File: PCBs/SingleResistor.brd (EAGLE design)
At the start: 10.2 x 39.5 mm, 3 parts

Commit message: Updated
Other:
- board size 10.2 x 39.5 mm -> 15 x 39.2 mm
- board text added: "PinwheelRobotics"
- board text added: "care@pinwheel.in"
- board text removed: "Pinwheel Robotics"
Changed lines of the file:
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@@
 <setting verticaltext="up"/>
 </settings>
-<grid distance="50" unitdist="mil" unit="mm" style="lines" multiple="1" display="yes" altdistance="5" altunitdist="mil" altunit="mm"/>
+<grid distance="0.5" unitdist="mm" unit="mm" style="lines" multiple="1" display="yes" altdistance="5" altunitdist="mil" altunit="mm"/>
 <layers>
 <layer number="1" name="Top" color="4" fill="1" visible="yes" active="yes"/>
@@
 <layer number="43" name="vRestrict" color="2" fill="10" visible="yes" active="yes"/>
 <layer number="44" name="Drills" color="7" fill="1" visible="no" active="yes"/>
-<layer number="45" name="Holes" color="7" fill="1" visible="no" active="yes"/>
+<layer number="45" name="Holes" color="7" fill="1" visible="yes" active="yes"/>
 <layer number="46" name="Milling" color="3" fill="1" visible="no" active="yes"/>
 <layer number="47" name="Measures" color="7" fill="1" visible="no" active="yes"/>
@@
 <board>
 <plain>
-<wire x1="6.35" y1="3.81" x2="16.5" y2="3.81" width="0" layer="20"/>
-<wire x1="16.5" y1="3.81" x2="16.5" y2="43.307" width="0" layer="20"/>
-<wire x1="16.5" y1="43.307" x2="6.35" y2="43.297" width="0" layer="20"/>
-<wire x1="6.35" y1="43.297" x2="6.35" y2="3.81" width="0" layer="20"/>
-<text x="15.494" y="20.32" size="0.8128" layer="21" rot="R90">Pinwheel Robotics </text>
+<wire x1="4" y1="41.2811875" x2="4" y2="6.123309375" width="0" layer="20"/>
+<wire x1="4" y1="6.123309375" x2="6.059309375" y2="4.064" width="0" layer="20" curve="90"/>
+<wire x1="6.059309375" y1="4.064" x2="16.70208125" y2="4.064" width="0" layer="20"/>
+<wire x1="16.70208125" y1="4.064" x2="19" y2="6.36191875" width="0" layer="20" curve="90"/>
+<wire x1="19" y1="6.36191875" x2="19" y2="41.058371875" width="0" layer="20"/>
+<wire x1="19" y1="41.058371875" x2="16.751375" y2="43.3055" width="0" layer="20" curve="90.038166"/>
+<wire x1="16.751375" y1="43.3055" x2="6.0158125" y2="43.29834375" width="0" layer="20"/>
+<wire x1="6.0158125" y1="43.29834375" x2="4" y2="41.2811875" width="0" layer="20" curve="89.999088"/>
+<hole x="6.065" y="41.185" drill="3"/>
+<hole x="16.774" y="41.304" drill="3"/>
+<hole x="5.938" y="6.057" drill="3"/>
+<hole x="16.945" y="5.987" drill="3"/>
+<text x="6.5" y="16.5" size="1.778" layer="21" rot="R90">PinwheelRobotics</text>
+<text x="17" y="34" size="1.778" layer="22" rot="MR270">care@pinwheel.in</text>
 </plain>
 <attributes>

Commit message: New Update
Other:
- outline, holes or cut-outs redrawn
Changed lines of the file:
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@@
 <board>
 <plain>
-<wire x1="4" y1="41.2811875" x2="4" y2="6.123309375" width="0" layer="20"/>
-<wire x1="4" y1="6.123309375" x2="6.059309375" y2="4.064" width="0" layer="20" curve="90"/>
-<wire x1="6.059309375" y1="4.064" x2="16.70208125" y2="4.064" width="0" layer="20"/>
-<wire x1="16.70208125" y1="4.064" x2="19" y2="6.36191875" width="0" layer="20" curve="90"/>
-<wire x1="19" y1="6.36191875" x2="19" y2="41.058371875" width="0" layer="20"/>
-<wire x1="19" y1="41.058371875" x2="16.751375" y2="43.3055" width="0" layer="20" curve="90.038166"/>
-<wire x1="16.751375" y1="43.3055" x2="6.0158125" y2="43.29834375" width="0" layer="20"/>
-<wire x1="6.0158125" y1="43.29834375" x2="4" y2="41.2811875" width="0" layer="20" curve="89.999088"/>
-<hole x="6.065" y="41.185" drill="3"/>
-<hole x="16.774" y="41.304" drill="3"/>
-<hole x="5.938" y="6.057" drill="3"/>
-<hole x="16.945" y="5.987" drill="3"/>
+<wire x1="4" y1="42.358221875" x2="4" y2="5.791765625" width="0" layer="20"/>
+<wire x1="4" y1="5.791765625" x2="5.727765625" y2="4.064" width="0" layer="20" curve="90"/>
+<wire x1="5.727765625" y1="4.064" x2="16.91804375" y2="4.064" width="0" layer="20"/>
+<wire x1="16.91804375" y1="4.064" x2="19" y2="6.14595625" width="0" layer="20" curve="90"/>
+<wire x1="19" y1="6.14595625" x2="19" y2="42.09330625" width="0" layer="20"/>
+<wire x1="19" y1="42.09330625" x2="17.78630625" y2="43.306190625" width="0" layer="20" curve="90.038234"/>
+<wire x1="17.78630625" y1="43.306190625" x2="4.938778125" y2="43.297625" width="0" layer="20"/>
+<wire x1="4.938778125" y1="43.297625" x2="4" y2="42.358221875" width="0" layer="20" curve="90.077877"/>
+<hole x="6" y="41" drill="3"/>
+<hole x="17" y="41" drill="3"/>
+<hole x="6" y="6.5" drill="3"/>
+<hole x="17" y="6.5" drill="3"/>
 <text x="6.5" y="16.5" size="1.778" layer="21" rot="R90">PinwheelRobotics</text>
 <text x="17" y="34" size="1.778" layer="22" rot="MR270">care@pinwheel.in</text>

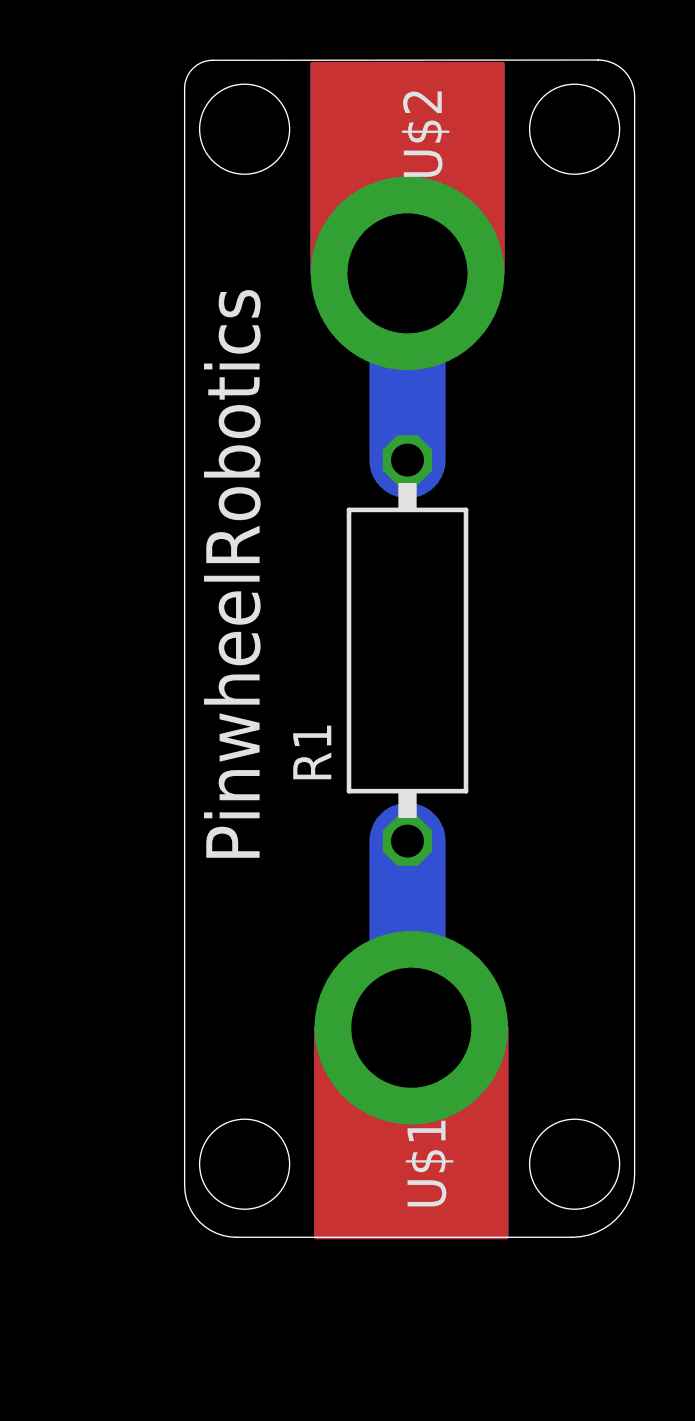
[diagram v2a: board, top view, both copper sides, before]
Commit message: New Update for board curv
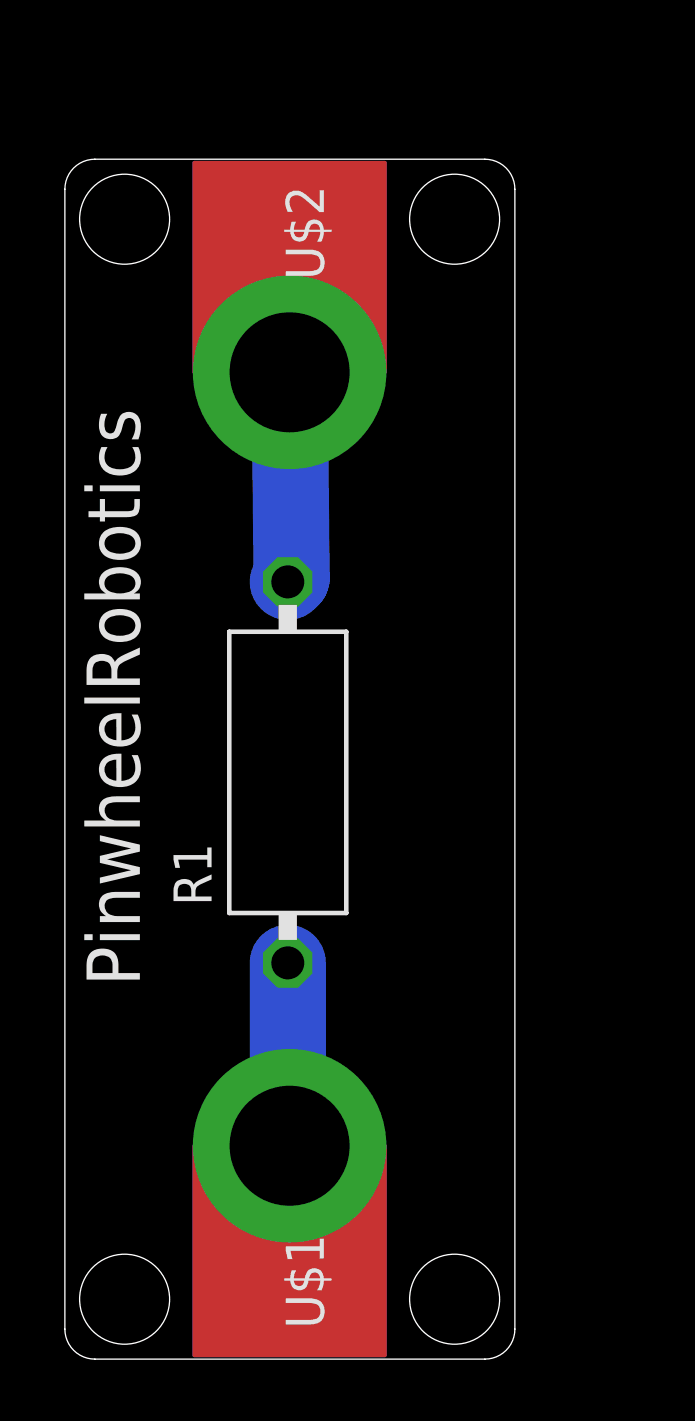
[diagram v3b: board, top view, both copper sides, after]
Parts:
- moved R1 5.69 mm to (7.44, 19.6)
- moved U$1 5.65 mm to (7.50, 7.12)
- moved U$2 5.13 mm to (7.50, 32.9)
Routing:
- net N$2: track 6.22 -> 7.04 mm
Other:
- board size 15 x 39.2 mm -> 15 x 40 mm
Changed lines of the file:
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@@
 <layer number="44" name="Drills" color="7" fill="1" visible="no" active="yes"/>
 <layer number="45" name="Holes" color="7" fill="1" visible="yes" active="yes"/>
-<layer number="46" name="Milling" color="3" fill="1" visible="no" active="yes"/>
+<layer number="46" name="Milling" color="3" fill="1" visible="yes" active="yes"/>
 <layer number="47" name="Measures" color="7" fill="1" visible="no" active="yes"/>
 <layer number="48" name="Document" color="7" fill="1" visible="yes" active="yes"/>
@@
 <board>
 <plain>
-<wire x1="4" y1="42.358221875" x2="4" y2="5.791765625" width="0" layer="20"/>
-<wire x1="4" y1="5.791765625" x2="5.727765625" y2="4.064" width="0" layer="20" curve="90"/>
-<wire x1="5.727765625" y1="4.064" x2="16.91804375" y2="4.064" width="0" layer="20"/>
-<wire x1="16.91804375" y1="4.064" x2="19" y2="6.14595625" width="0" layer="20" curve="90"/>
-<wire x1="19" y1="6.14595625" x2="19" y2="42.09330625" width="0" layer="20"/>
-<wire x1="19" y1="42.09330625" x2="17.78630625" y2="43.306190625" width="0" layer="20" curve="90.038234"/>
-<wire x1="17.78630625" y1="43.306190625" x2="4.938778125" y2="43.297625" width="0" layer="20"/>
-<wire x1="4.938778125" y1="43.297625" x2="4" y2="42.358221875" width="0" layer="20" curve="90.077877"/>
-<hole x="6" y="41" drill="3"/>
-<hole x="17" y="41" drill="3"/>
-<hole x="6" y="6.5" drill="3"/>
-<hole x="17" y="6.5" drill="3"/>
-<text x="6.5" y="16.5" size="1.778" layer="21" rot="R90">PinwheelRobotics</text>
-<text x="17" y="34" size="1.778" layer="22" rot="MR270">care@pinwheel.in</text>
+<wire x1="14.009" y1="40" x2="1.009" y2="40" width="0" layer="20"/>
+<wire x1="1.009" y1="40" x2="0.009" y2="39" width="0" layer="20" curve="90"/>
+<wire x1="0.009" y1="39" x2="0.009" y2="1.003" width="0" layer="20"/>
+<wire x1="0.009" y1="1.003" x2="1.009" y2="0.003" width="0" layer="20" curve="90"/>
+<wire x1="1.009" y1="0.003" x2="14.009" y2="0.003" width="0" layer="20"/>
+<wire x1="14.009" y1="0.003" x2="15.009" y2="1.003" width="0" layer="20" curve="90"/>
+<wire x1="15.009" y1="1.003" x2="15.009" y2="39" width="0" layer="20"/>
+<wire x1="15.009" y1="39" x2="14.009" y2="40" width="0" layer="20" curve="90"/>
+<hole x="2" y="38" drill="3"/>
+<hole x="13" y="38" drill="3"/>
+<hole x="2" y="2" drill="3"/>
+<hole x="13" y="2" drill="3"/>
+<text x="2.509" y="12.439" size="1.778" layer="21" rot="R90">PinwheelRobotics</text>
+<text x="13.009" y="29.939" size="1.778" layer="22" rot="MR270">care@pinwheel.in</text>
 </plain>
 <attributes>
@@
 </autorouter>
 <elements>
-<element name="R1" library="rcl" library_urn="urn:adsk.eagle:library:334" package="VMTB60" package3d_urn="urn:adsk.eagle:package:26122/2" value="" x="11.43" y="23.622" smashed="yes" rot="R90">
-<attribute name="NAME" x="8.89" y="19.177" size="1.27" layer="25" ratio="10" rot="R90"/>
-<attribute name="POPULARITY" value="0" x="29.21" y="43.942" size="1.778" layer="27" rot="R90" display="off"/>
-<attribute name="SPICEPREFIX" value="R" x="29.21" y="43.942" size="1.778" layer="27" rot="R90" display="off"/>
-<attribute name="VALUE" x="12.065" y="19.177" size="1.27" layer="27" ratio="10" rot="R90"/>
+<element name="R1" library="rcl" library_urn="urn:adsk.eagle:library:334" package="VMTB60" package3d_urn="urn:adsk.eagle:package:26122/2" value="" x="7.439" y="19.561" smashed="yes" rot="R90">
+<attribute name="NAME" x="4.899" y="15.116" size="1.27" layer="25" ratio="10" rot="R90"/>
+<attribute name="POPULARITY" value="0" x="25.219" y="39.881" size="1.778" layer="27" rot="R90" display="off"/>
+<attribute name="SPICEPREFIX" value="R" x="25.219" y="39.881" size="1.778" layer="27" rot="R90" display="off"/>
+<attribute name="VALUE" x="8.074" y="15.116" size="1.27" layer="27" ratio="10" rot="R90"/>
 </element>
-<element name="U$2" library="microbit" package="MICROBIT_PAD" value="MICROBIT_PAD" x="11.43" y="36.195" smashed="yes" rot="R180">
-<attribute name="NAME" x="11.303" y="42.418" size="1.27" layer="21" rot="R270"/>
+<element name="U$2" library="microbit" package="MICROBIT_PAD" value="MICROBIT_PAD" x="7.5" y="32.896" smashed="yes" rot="R180">
+<attribute name="NAME" x="7.373" y="39.119" size="1.27" layer="21" rot="R270"/>
 </element>
-<element name="U$1" library="microbit" package="MICROBIT_PAD" value="MICROBIT_PAD" x="11.557" y="11.049" smashed="yes">
-<attribute name="NAME" x="12.7" y="4.953" size="1.27" layer="21" rot="R90"/>
+<element name="U$1" library="microbit" package="MICROBIT_PAD" value="MICROBIT_PAD" x="7.5" y="7.115" smashed="yes">
+<attribute name="NAME" x="8.643" y="1.019" size="1.27" layer="21" rot="R90"/>
 </element>
 </elements>
@@
 <contactref element="R1" pad="1"/>
 <contactref element="U$1" pad="PAD"/>
-<wire x1="11.43" y1="17.272" x2="11.43" y2="10.16" width="2.54" layer="16"/>
-<wire x1="11.43" y1="10.16" x2="11.557" y2="11.049" width="0" layer="19" extent="16-16"/>
+<wire x1="7.439" y1="13.211" x2="7.439" y2="6" width="2.54" layer="16"/>
+<wire x1="7.439" y1="6" x2="7.5" y2="7.115" width="0" layer="19" extent="16-16"/>
 </signal>
 <signal name="N$2">
 <contactref element="U$2" pad="PAD"/>
 <contactref element="R1" pad="2"/>
-<wire x1="11.43" y1="36.195" x2="11.43" y2="29.972" width="2.54" layer="16"/>
+<wire x1="7.5" y1="32.896" x2="7.566" y2="26.038" width="2.54" layer="16"/>
+<wire x1="7.566" y1="26.038" x2="7.439" y2="25.911" width="2.54" layer="16"/>
 </signal>
 </signals>

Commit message: Dimension added
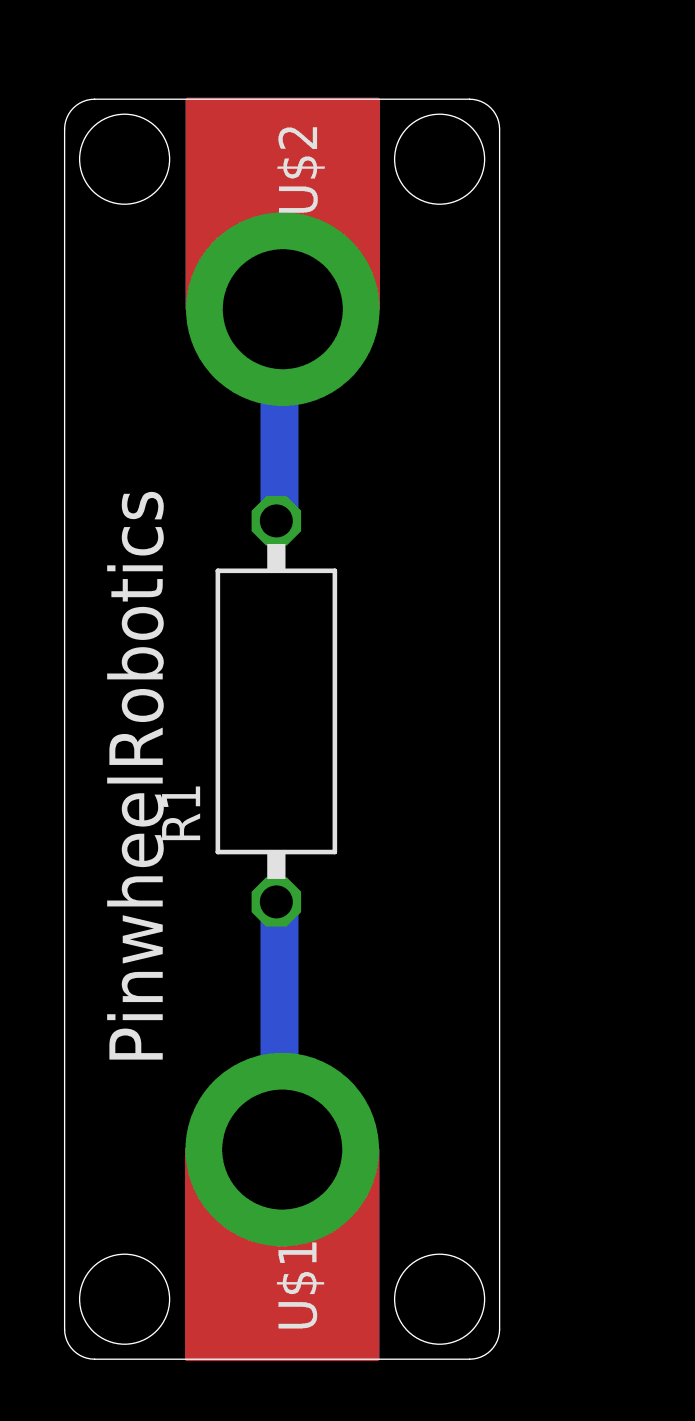
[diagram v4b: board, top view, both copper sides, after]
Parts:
- moved U$2 2.12 mm to (7.27, 35.0)
- moved R1 2.07 mm to (7.06, 21.6)
- moved U$1 0.28 mm to (7.25, 6.99)
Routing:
- net N$1: track 7.21 -> 8.43 mm
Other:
- board size 15 x 40 mm -> 14.5 x 42 mm
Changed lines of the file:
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@@
 <board>
 <plain>
-<wire x1="14.009" y1="40" x2="1.009" y2="40" width="0" layer="20"/>
-<wire x1="1.009" y1="40" x2="0.009" y2="39" width="0" layer="20" curve="90"/>
-<wire x1="0.009" y1="39" x2="0.009" y2="1.003" width="0" layer="20"/>
-<wire x1="0.009" y1="1.003" x2="1.009" y2="0.003" width="0" layer="20" curve="90"/>
-<wire x1="1.009" y1="0.003" x2="14.009" y2="0.003" width="0" layer="20"/>
-<wire x1="14.009" y1="0.003" x2="15.009" y2="1.003" width="0" layer="20" curve="90"/>
-<wire x1="15.009" y1="1.003" x2="15.009" y2="39" width="0" layer="20"/>
-<wire x1="15.009" y1="39" x2="14.009" y2="40" width="0" layer="20" curve="90"/>
-<hole x="2" y="38" drill="3"/>
-<hole x="13" y="38" drill="3"/>
+<wire x1="1" y1="0" x2="13.5" y2="0" width="0" layer="20"/>
+<wire x1="13.5" y1="0" x2="14.5" y2="1" width="0" layer="20" curve="90"/>
+<wire x1="14.5" y1="1" x2="14.5" y2="41" width="0" layer="20"/>
+<wire x1="14.5" y1="41" x2="13.5" y2="42" width="0" layer="20" curve="90"/>
+<wire x1="13.5" y1="42" x2="1" y2="42" width="0" layer="20"/>
+<wire x1="1" y1="42" x2="0" y2="41" width="0" layer="20" curve="90"/>
+<wire x1="0" y1="41" x2="0" y2="1" width="0" layer="20"/>
+<wire x1="0" y1="1" x2="1" y2="0" width="0" layer="20" curve="90"/>
+<hole x="2" y="40" drill="3"/>
+<hole x="12.5" y="40" drill="3"/>
 <hole x="2" y="2" drill="3"/>
-<hole x="13" y="2" drill="3"/>
-<text x="2.509" y="12.439" size="1.778" layer="21" rot="R90">PinwheelRobotics</text>
-<text x="13.009" y="29.939" size="1.778" layer="22" rot="MR270">care@pinwheel.in</text>
+<hole x="12.5" y="2" drill="3"/>
+<text x="3.271" y="9.772" size="1.778" layer="21" rot="R90">PinwheelRobotics</text>
+<text x="12.509" y="29.939" size="1.778" layer="22" rot="MR270">care@pinwheel.in</text>
 </plain>
 <attributes>
@@
 </autorouter>
 <elements>
-<element name="R1" library="rcl" library_urn="urn:adsk.eagle:library:334" package="VMTB60" package3d_urn="urn:adsk.eagle:package:26122/2" value="" x="7.439" y="19.561" smashed="yes" rot="R90">
-<attribute name="NAME" x="4.899" y="15.116" size="1.27" layer="25" ratio="10" rot="R90"/>
-<attribute name="POPULARITY" value="0" x="25.219" y="39.881" size="1.778" layer="27" rot="R90" display="off"/>
-<attribute name="SPICEPREFIX" value="R" x="25.219" y="39.881" size="1.778" layer="27" rot="R90" display="off"/>
-<attribute name="VALUE" x="8.074" y="15.116" size="1.27" layer="27" ratio="10" rot="R90"/>
+<element name="R1" library="rcl" library_urn="urn:adsk.eagle:library:334" package="VMTB60" package3d_urn="urn:adsk.eagle:package:26122/2" value="" x="7.058" y="21.593" smashed="yes" rot="R90">
+<attribute name="NAME" x="4.518" y="17.148" size="1.27" layer="25" ratio="10" rot="R90"/>
+<attribute name="POPULARITY" value="0" x="24.838" y="41.913" size="1.778" layer="27" rot="R90" display="off"/>
+<attribute name="SPICEPREFIX" value="R" x="24.838" y="41.913" size="1.778" layer="27" rot="R90" display="off"/>
+<attribute name="VALUE" x="7.693" y="17.148" size="1.27" layer="27" ratio="10" rot="R90"/>
 </element>
-<element name="U$2" library="microbit" package="MICROBIT_PAD" value="MICROBIT_PAD" x="7.5" y="32.896" smashed="yes" rot="R180">
-<attribute name="NAME" x="7.373" y="39.119" size="1.27" layer="21" rot="R270"/>
+<element name="U$2" library="microbit" package="MICROBIT_PAD" value="MICROBIT_PAD" x="7.273" y="35" smashed="yes" rot="R180">
+<attribute name="NAME" x="7.146" y="41.223" size="1.27" layer="21" rot="R270"/>
 </element>
-<element name="U$1" library="microbit" package="MICROBIT_PAD" value="MICROBIT_PAD" x="7.5" y="7.115" smashed="yes">
-<attribute name="NAME" x="8.643" y="1.019" size="1.27" layer="21" rot="R90"/>
+<element name="U$1" library="microbit" package="MICROBIT_PAD" value="MICROBIT_PAD" x="7.254" y="6.988" smashed="yes">
+<attribute name="NAME" x="8.397" y="0.892" size="1.27" layer="21" rot="R90"/>
 </element>
 </elements>
@@
 <contactref element="R1" pad="1"/>
 <contactref element="U$1" pad="PAD"/>
-<wire x1="7.439" y1="13.211" x2="7.439" y2="6" width="2.54" layer="16"/>
-<wire x1="7.439" y1="6" x2="7.5" y2="7.115" width="0" layer="19" extent="16-16"/>
+<wire x1="7.1628" y1="7.0104" x2="7.1628" y2="15.24" width="1.27" layer="16"/>
+<wire x1="7.1628" y1="15.24" x2="7.058" y2="15.243" width="0.1524" layer="16"/>
+<wire x1="7.1628" y1="7.0104" x2="7.254" y2="6.988" width="0.1524" layer="16"/>
 </signal>
 <signal name="N$2">
 <contactref element="U$2" pad="PAD"/>
 <contactref element="R1" pad="2"/>
-<wire x1="7.5" y1="32.896" x2="7.566" y2="26.038" width="2.54" layer="16"/>
-<wire x1="7.566" y1="26.038" x2="7.439" y2="25.911" width="2.54" layer="16"/>
+<wire x1="7.1628" y1="34.8996" x2="7.1628" y2="28.0416" width="1.27" layer="16"/>
+<wire x1="7.1628" y1="28.0416" x2="7.058" y2="27.943" width="0.1524" layer="16"/>
+<wire x1="7.1628" y1="34.8996" x2="7.273" y2="35" width="0.1524" layer="16"/>
 </signal>
 </signals>
